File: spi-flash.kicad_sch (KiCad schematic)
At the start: 2 parts, among them J4 Tag-Connect_TC2050-IDC-NL_2x5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, U7 AT25FF161A-MAHN-T

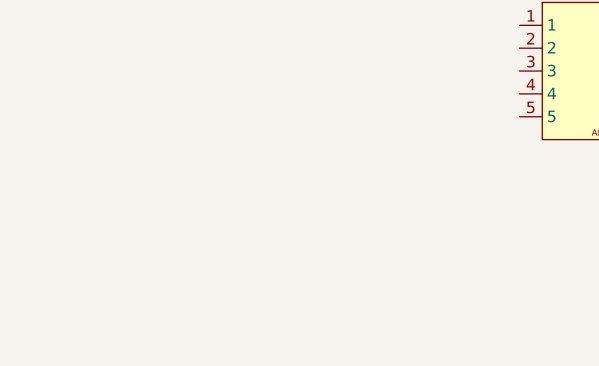
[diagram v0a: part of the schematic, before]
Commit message: [#94684] Add ports to subsheets
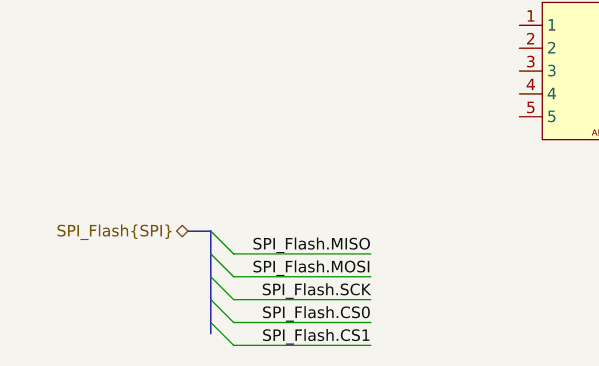
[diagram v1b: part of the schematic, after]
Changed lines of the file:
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@@
 	(generator "eeschema")
 	(generator_version "9.0")
-	(paper "A4")
+	(paper "A3")
 	(title_block
 		(title "renode-reference-platform")
@@
 		)
 	)
+	(bus_entry
+		(at 77.47 114.3)
+		(size 2.54 2.54)
+		(stroke
+			(width 0)
+			(type default)
+		)
+	)
+	(bus_entry
+		(at 77.47 111.76)
+		(size 2.54 2.54)
+		(stroke
+			(width 0)
+			(type default)
+		)
+	)
+	(bus_entry
+		(at 77.47 119.38)
+		(size 2.54 2.54)
+		(stroke
+			(width 0)
+			(type default)
+		)
+	)
+	(bus_entry
+		(at 77.47 116.84)
+		(size 2.54 2.54)
+		(stroke
+			(width 0)
+			(type default)
+		)
+	)
+	(bus_entry
+		(at 77.47 109.22)
+		(size 2.54 2.54)
+		(stroke
+			(width 0)
+			(type default)
+		)
+	)
+	(bus
+		(pts
+			(xy 74.93 109.22) (xy 77.47 109.22)
+		)
+		(stroke
+			(width 0)
+			(type default)
+		)
+	)
+	(bus
+		(pts
+			(xy 77.47 119.38) (xy 77.47 120.65)
+		)
+		(stroke
+			(width 0)
+			(type default)
+		)
+	)
+	(wire
+		(pts
+			(xy 95.25 121.92) (xy 80.01 121.92)
+		)
+		(stroke
+			(width 0)
+			(type default)
+		)
+	)
+	(wire
+		(pts
+			(xy 95.25 111.76) (xy 80.01 111.76)
+		)
+		(stroke
+			(width 0)
+			(type default)
+		)
+	)
+	(wire
+		(pts
+			(xy 95.25 116.84) (xy 80.01 116.84)
+		)
+		(stroke
+			(width 0)
+			(type default)
+		)
+	)
+	(wire
+		(pts
+			(xy 95.25 119.38) (xy 80.01 119.38)
+		)
+		(stroke
+			(width 0)
+			(type default)
+		)
+	)
+	(wire
+		(pts
+			(xy 95.25 114.3) (xy 80.01 114.3)
+		)
+		(stroke
+			(width 0)
+			(type default)
+		)
+	)
+	(bus
+		(pts
+			(xy 77.47 111.76) (xy 77.47 114.3)
+		)
+		(stroke
+			(width 0)
+			(type default)
+		)
+	)
+	(bus
+		(pts
+			(xy 77.47 109.22) (xy 77.47 111.76)
+		)
+		(stroke
+			(width 0)
+			(type default)
+		)
+	)
+	(bus
+		(pts
+			(xy 77.47 116.84) (xy 77.47 119.38)
+		)
+		(stroke
+			(width 0)
+			(type default)
+		)
+	)
+	(bus
+		(pts
+			(xy 77.47 114.3) (xy 77.47 116.84)
+		)
+		(stroke
+			(width 0)
+			(type default)
+		)
+	)
+	(label "SPI_Flash.MISO"
+		(at 95.25 111.76 180)
+		(effects
+			(font
+				(size 1.27 1.27)
+			)
+			(justify right bottom)
+		)
+	)
+	(label "SPI_Flash.CS1"
+		(at 95.25 121.92 180)
+		(effects
+			(font
+				(size 1.27 1.27)
+			)
+			(justify right bottom)
+		)
+	)
+	(label "SPI_Flash.SCK"
+		(at 95.25 116.84 180)
+		(effects
+			(font
+				(size 1.27 1.27)
+			)
+			(justify right bottom)
+		)
+	)
+	(label "SPI_Flash.CS0"
+		(at 95.25 119.38 180)
+		(effects
+			(font
+				(size 1.27 1.27)
+			)
+			(justify right bottom)
+		)
+	)
+	(label "SPI_Flash.MOSI"
+		(at 95.25 114.3 180)
+		(effects
+			(font
+				(size 1.27 1.27)
+			)
+			(justify right bottom)
+		)
+	)
+	(hierarchical_label "SPI_Flash{SPI}"
+		(shape bidirectional)
+		(at 74.93 109.22 180)
+		(effects
+			(font
+				(size 1.27 1.27)
+			)
+			(justify right)
+		)
+	)

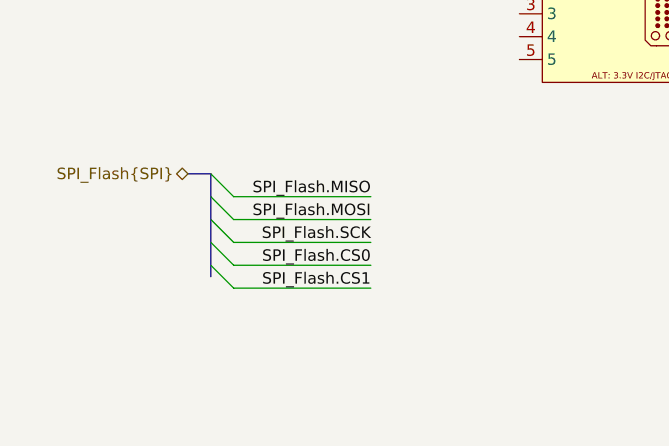
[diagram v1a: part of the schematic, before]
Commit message: [#94727] Add RMII, IOs, JTAG, UART, QSPI connection to MCU
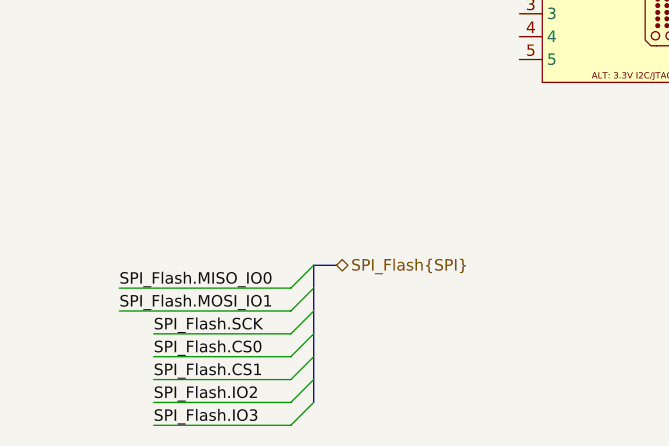
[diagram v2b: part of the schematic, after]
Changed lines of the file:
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@@
 	)
 	(bus_entry
-		(at 77.47 114.3)
-		(size 2.54 2.54)
-		(stroke
-			(width 0)
-			(type default)
-		)
-	)
-	(bus_entry
-		(at 77.47 111.76)
-		(size 2.54 2.54)
-		(stroke
-			(width 0)
-			(type default)
-		)
-	)
-	(bus_entry
-		(at 77.47 119.38)
-		(size 2.54 2.54)
-		(stroke
-			(width 0)
-			(type default)
-		)
-	)
-	(bus_entry
-		(at 77.47 116.84)
-		(size 2.54 2.54)
-		(stroke
-			(width 0)
-			(type default)
-		)
-	)
-	(bus_entry
-		(at 77.47 109.22)
-		(size 2.54 2.54)
-		(stroke
-			(width 0)
-			(type default)
-		)
-	)
-	(bus
-		(pts
-			(xy 74.93 109.22) (xy 77.47 109.22)
-		)
-		(stroke
-			(width 0)
-			(type default)
-		)
-	)
-	(bus
-		(pts
-			(xy 77.47 119.38) (xy 77.47 120.65)
-		)
-		(stroke
-			(width 0)
-			(type default)
-		)
-	)
-	(wire
-		(pts
-			(xy 95.25 121.92) (xy 80.01 121.92)
-		)
-		(stroke
-			(width 0)
-			(type default)
-		)
-	)
-	(wire
-		(pts
-			(xy 95.25 111.76) (xy 80.01 111.76)
-		)
-		(stroke
-			(width 0)
-			(type default)
-		)
-	)
-	(wire
-		(pts
-			(xy 95.25 116.84) (xy 80.01 116.84)
-		)
-		(stroke
-			(width 0)
-			(type default)
-		)
-	)
-	(wire
-		(pts
-			(xy 95.25 119.38) (xy 80.01 119.38)
-		)
-		(stroke
-			(width 0)
-			(type default)
-		)
-	)
-	(wire
-		(pts
-			(xy 95.25 114.3) (xy 80.01 114.3)
-		)
-		(stroke
-			(width 0)
-			(type default)
-		)
-	)
-	(bus
-		(pts
-			(xy 77.47 111.76) (xy 77.47 114.3)
-		)
-		(stroke
-			(width 0)
-			(type default)
-		)
-	)
-	(bus
-		(pts
-			(xy 77.47 109.22) (xy 77.47 111.76)
-		)
-		(stroke
-			(width 0)
-			(type default)
-		)
-	)
-	(bus
-		(pts
-			(xy 77.47 116.84) (xy 77.47 119.38)
-		)
-		(stroke
-			(width 0)
-			(type default)
-		)
-	)
-	(bus
-		(pts
-			(xy 77.47 114.3) (xy 77.47 116.84)
-		)
-		(stroke
-			(width 0)
-			(type default)
-		)
-	)
-	(label "SPI_Flash.MISO"
-		(at 95.25 111.76 180)
-		(effects
-			(font
-				(size 1.27 1.27)
-			)
-			(justify right bottom)
+		(at 88.9 124.46)
+		(size -2.54 2.54)
+		(stroke
+			(width 0)
+			(type default)
+		)
+	)
+	(bus_entry
+		(at 88.9 127)
+		(size -2.54 2.54)
+		(stroke
+			(width 0)
+			(type default)
+		)
+	)
+	(bus_entry
+		(at 88.9 132.08)
+		(size -2.54 2.54)
+		(stroke
+			(width 0)
+			(type default)
+		)
+	)
+	(bus_entry
+		(at 88.9 121.92)
+		(size -2.54 2.54)
+		(stroke
+			(width 0)
+			(type default)
+		)
+	)
+	(bus_entry
+		(at 88.9 129.54)
+		(size -2.54 2.54)
+		(stroke
+			(width 0)
+			(type default)
+		)
+	)
+	(bus_entry
+		(at 88.9 119.38)
+		(size -2.54 2.54)
+		(stroke
+			(width 0)
+			(type default)
+		)
+	)
+	(bus_entry
+		(at 88.9 134.62)
+		(size -2.54 2.54)
+		(stroke
+			(width 0)
+			(type default)
+		)
+	)
+	(wire
+		(pts
+			(xy 71.12 134.62) (xy 86.36 134.62)
+		)
+		(stroke
+			(width 0)
+			(type default)
+		)
+	)
+	(bus
+		(pts
+			(xy 88.9 127) (xy 88.9 129.54)
+		)
+		(stroke
+			(width 0)
+			(type default)
+		)
+	)
+	(bus
+		(pts
+			(xy 88.9 119.38) (xy 88.9 121.92)
+		)
+		(stroke
+			(width 0)
+			(type default)
+		)
+	)
+	(wire
+		(pts
+			(xy 67.31 121.92) (xy 86.36 121.92)
+		)
+		(stroke
+			(width 0)
+			(type default)
+		)
+	)
+	(bus
+		(pts
+			(xy 88.9 121.92) (xy 88.9 124.46)
+		)
+		(stroke
+			(width 0)
+			(type default)
+		)
+	)
+	(wire
+		(pts
+			(xy 71.12 127) (xy 86.36 127)
+		)
+		(stroke
+			(width 0)
+			(type default)
+		)
+	)
+	(wire
+		(pts
+			(xy 71.12 137.16) (xy 86.36 137.16)
+		)
+		(stroke
+			(width 0)
+			(type default)
+		)
+	)
+	(wire
+		(pts
+			(xy 71.12 132.08) (xy 86.36 132.08)
+		)
+		(stroke
+			(width 0)
+			(type default)
+		)
+	)
+	(bus
+		(pts
+			(xy 88.9 124.46) (xy 88.9 127)
+		)
+		(stroke
+			(width 0)
+			(type default)
+		)
+	)
+	(wire
+		(pts
+			(xy 67.31 124.46) (xy 86.36 124.46)
+		)
+		(stroke
+			(width 0)
+			(type default)
+		)
+	)
+	(bus
+		(pts
+			(xy 88.9 132.08) (xy 88.9 134.62)
+		)
+		(stroke
+			(width 0)
+			(type default)
+		)
+	)
+	(wire
+		(pts
+			(xy 71.12 129.54) (xy 86.36 129.54)
+		)
+		(stroke
+			(width 0)
+			(type default)
+		)
+	)
+	(bus
+		(pts
+			(xy 91.44 119.38) (xy 88.9 119.38)
+		)
+		(stroke
+			(width 0)
+			(type default)
+		)
+	)
+	(bus
+		(pts
+			(xy 88.9 129.54) (xy 88.9 132.08)
+		)
+		(stroke
+			(width 0)
+			(type default)
+		)
+	)
+	(label "SPI_Flash.SCK"
+		(at 71.12 127 0)
+		(effects
+			(font
+				(size 1.27 1.27)
+			)
+			(justify left bottom)
+		)
+	)
+	(label "SPI_Flash.CS0"
+		(at 71.12 129.54 0)
+		(effects
+			(font
+				(size 1.27 1.27)
+			)
+			(justify left bottom)
 		)
 	)
 	(label "SPI_Flash.CS1"
-		(at 95.25 121.92 180)
-		(effects
-			(font
-				(size 1.27 1.27)
-			)
-			(justify right bottom)
-		)
-	)
-	(label "SPI_Flash.SCK"
-		(at 95.25 116.84 180)
-		(effects
-			(font
-				(size 1.27 1.27)
-			)
-			(justify right bottom)
-		)
-	)
-	(label "SPI_Flash.CS0"
-		(at 95.25 119.38 180)
-		(effects
-			(font
-				(size 1.27 1.27)
-			)
-			(justify right bottom)
-		)
-	)
-	(label "SPI_Flash.MOSI"
-		(at 95.25 114.3 180)
-		(effects
-			(font
-				(size 1.27 1.27)
-			)
-			(justify right bottom)
+		(at 71.12 132.08 0)
+		(effects
+			(font
+				(size 1.27 1.27)
+			)
+			(justify left bottom)
+		)
+	)
+	(label "SPI_Flash.MOSI_IO1"
+		(at 67.31 124.46 0)
+		(effects
+			(font
+				(size 1.27 1.27)
+			)
+			(justify left bottom)
+		)
+	)
+	(label "SPI_Flash.IO3"
+		(at 71.12 137.16 0)
+		(effects
+			(font
+				(size 1.27 1.27)
+			)
+			(justify left bottom)
+		)
+	)
+	(label "SPI_Flash.IO2"
+		(at 71.12 134.62 0)
+		(effects
+			(font
+				(size 1.27 1.27)
+			)
+			(justify left bottom)
+		)
+	)
+	(label "SPI_Flash.MISO_IO0"
+		(at 67.31 121.92 0)
+		(effects
+			(font
+				(size 1.27 1.27)
+			)
+			(justify left bottom)
 		)
 	)
 	(hierarchical_label "SPI_Flash{SPI}"
 		(shape bidirectional)
-		(at 74.93 109.22 180)
-		(effects
-			(font
-				(size 1.27 1.27)
-			)
-			(justify right)
-		)
-	)
+		(at 91.44 119.38 0)
+		(effects
+			(font
+				(size 1.27 1.27)
+			)
+			(justify left)
+		)
+	)

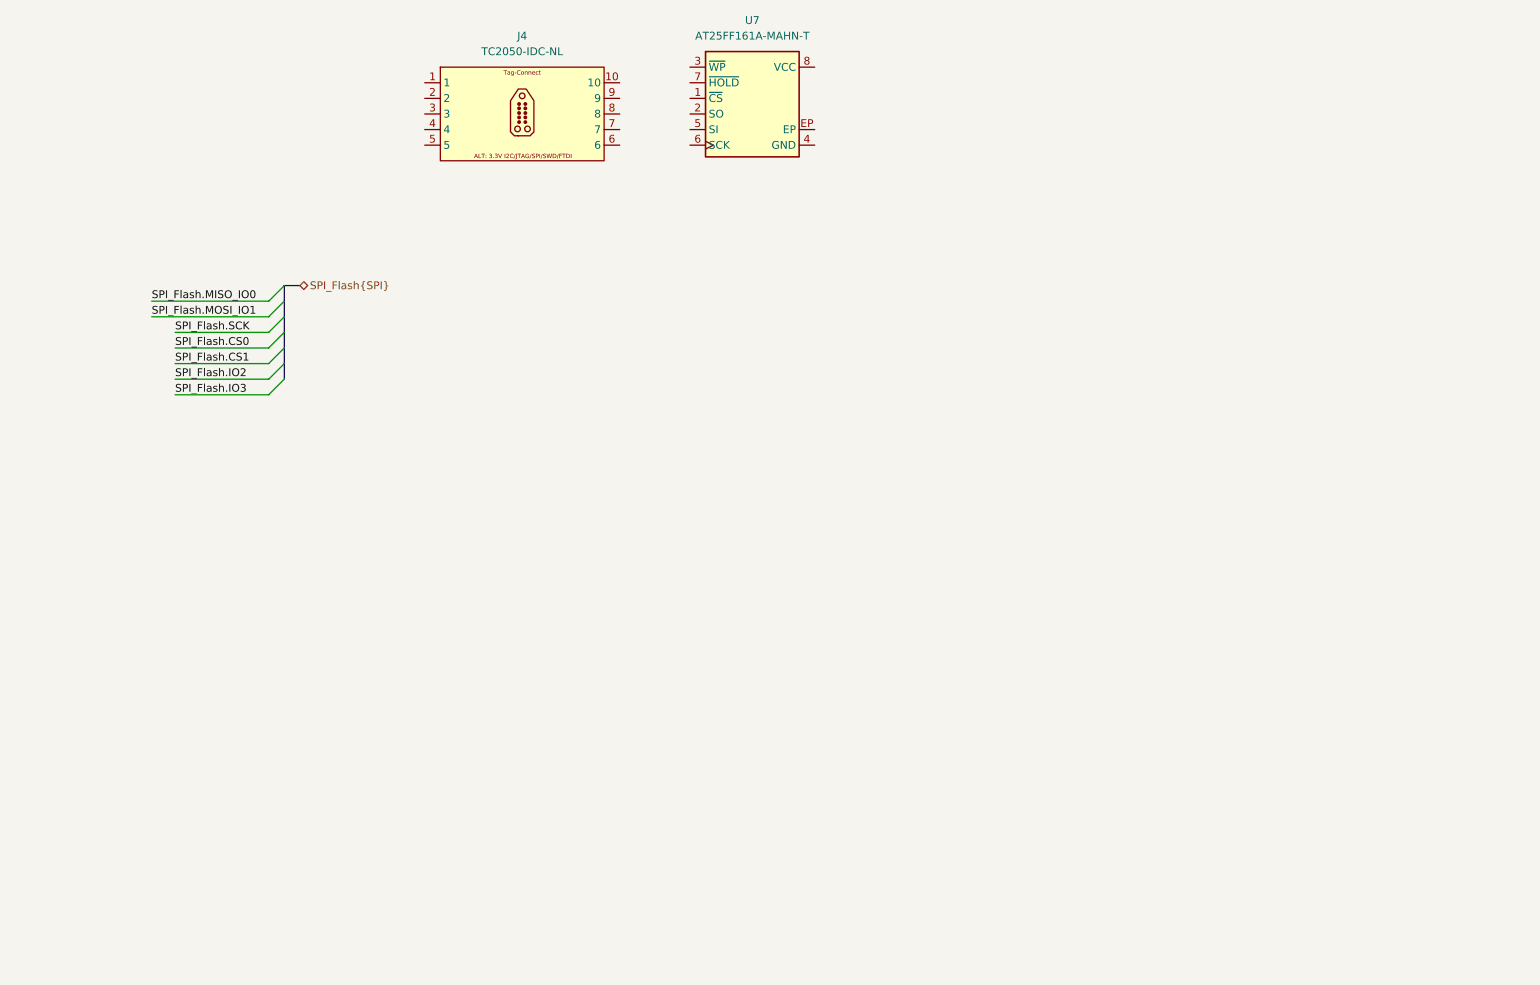
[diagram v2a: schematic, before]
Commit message: [#94972] Add QSPI flash
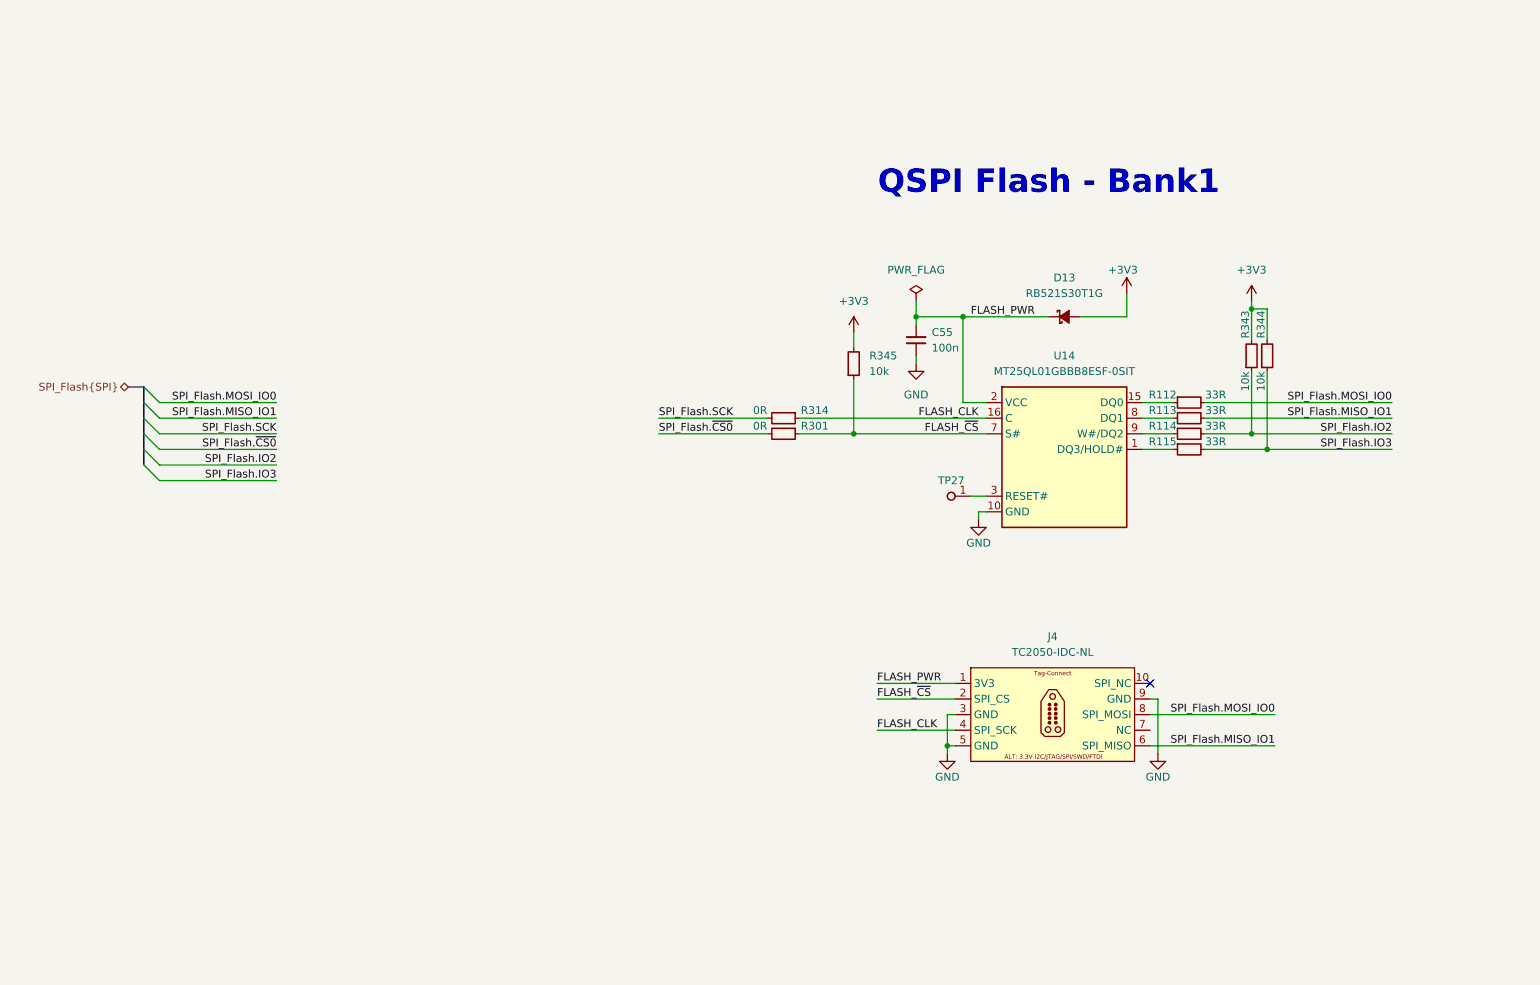
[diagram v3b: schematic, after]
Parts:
- removed U7: AT25FF161A-MAHN-T, antmicro-footprints:USON-8_2x3mm_P0.5mm, symbol antmicroMemory:AT25FF161A-MAHN-T
- added C55: C_100n_0402, antmicro-footprints:C_0402_1005Metric, symbol antmicroCapacitors0402:C_100n_0402
- added D13: RB521S30T1G, antmicro-footprints:SOD-523, symbol antmicroDiodesRectifiersSingle:RB521S30T1G
- added R112, R113, R114, R115: R_33R_0402, antmicro-footprints:R_0402_1005Metric, symbol antmicroResistors0402:R_33R_0402
- added R301, R314: R_0R_0402, antmicro-footprints:R_0402_1005Metric, symbol antmicroResistors0402:R_0R_0402
- added R343, R344, R345: R_10k_0402, antmicro-footprints:R_0402_1005Metric, symbol antmicroResistors0402:R_10k_0402
- added TP27: TP_1mm_SMD, antmicro-footprints:TP_SMD_1mm, symbol antmicroTestPoints:TP_1mm_SMD
- added U14: MT25QL01GBBB8E_SOP2-16, antmicro-footprints:SOP2-16_7.5x10.3mm, symbol antmicroMemory:MT25QL01GBBB8E_SOP2-16
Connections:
- net SPI_Flash.IO2: now also R114.2, R343.1
- net SPI_Flash.IO3: now also R115.2, R344.1
- net SPI_Flash.SCK: now also R314.2
- net FLASH_PWR: now reaches J4.1
- net FLASH_PWR: now also C55.2, D13.1 (C), U14.2 (VCC)
- net FLASH_~{CS}: now reaches J4.2
- net FLASH_~{CS}: now also R301.1, R345.1, U14.7 (S#)
- net GND: now reaches J4.3
- net GND: now also J4.5, J4.9, C55.1, U14.10 (GND)
- net FLASH_CLK: now reaches J4.4
- net FLASH_CLK: now also R314.1, U14.16 (C)
- net SPI_Flash.MISO_IO1: now reaches J4.6
- net SPI_Flash.MISO_IO1: now also R113.2
- net SPI_Flash.MOSI_IO0: now reaches J4.8
- net SPI_Flash.MOSI_IO0: now also R112.2
- new net: R112.1, U14.15 (DQ0)
- new net: R115.1, U14.1 (DQ3/HOLD#)
- new net: TP27.1, U14.3 (RESET#)
- new net: R113.1, U14.8 (DQ1)
- new net: R114.1, U14.9 (W#/DQ2)
- new net +3V3: D13.2 (A), R343.2, R344.2, R345.2
- new net SPI_Flash.~{CS0}: R301.2
- no-connect marks 0 -> 1
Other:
- note added: "QSPI Flash - Bank1"
- moved on the sheet: J4

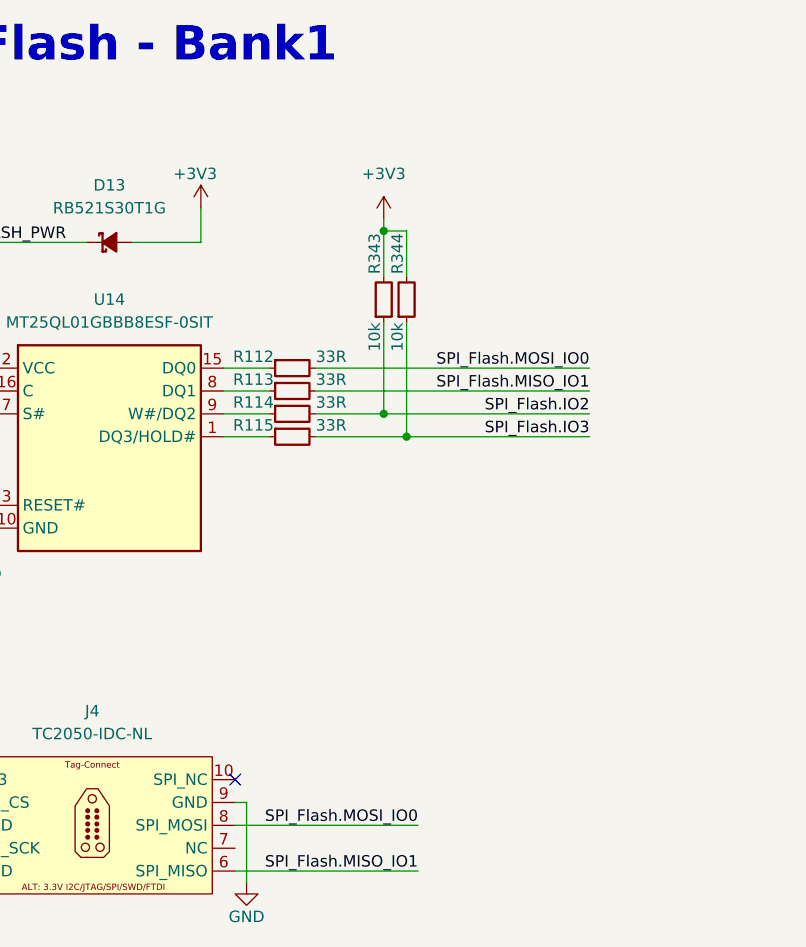
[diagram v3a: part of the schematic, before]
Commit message: [#95036] Add testpoints
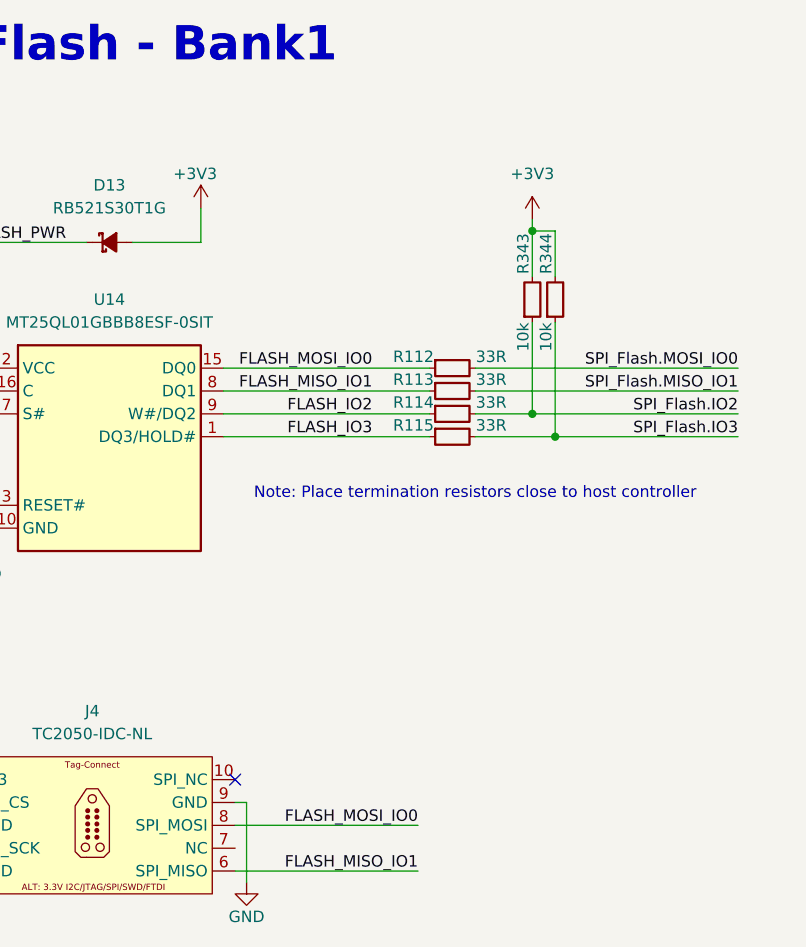
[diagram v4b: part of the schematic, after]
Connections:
- net SPI_Flash.MISO_IO1: no longer J4.6
- net SPI_Flash.MOSI_IO0: no longer J4.8
- net FLASH_MOSI_IO0: now reaches R112.1, U14.15 (DQ0)
- net FLASH_MOSI_IO0: now also J4.8
- net FLASH_IO3: now reaches R115.1, U14.1 (DQ3/HOLD#)
- net FLASH_MISO_IO1: now reaches R113.1, U14.8 (DQ1)
- net FLASH_MISO_IO1: now also J4.6
- net FLASH_IO2: now reaches R114.1, U14.9 (W#/DQ2)
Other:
- note added: "Note: Place termination resistors close to host controller"
- moved on the sheet: R112, R113, R114, R115, R343, R344

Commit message: [#95398] Schematic cleanup
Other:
- moved on the sheet: R301, R314
